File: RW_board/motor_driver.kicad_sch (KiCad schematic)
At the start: 24 parts, among them IC1 MCT8316Z0RQRGFRQ1

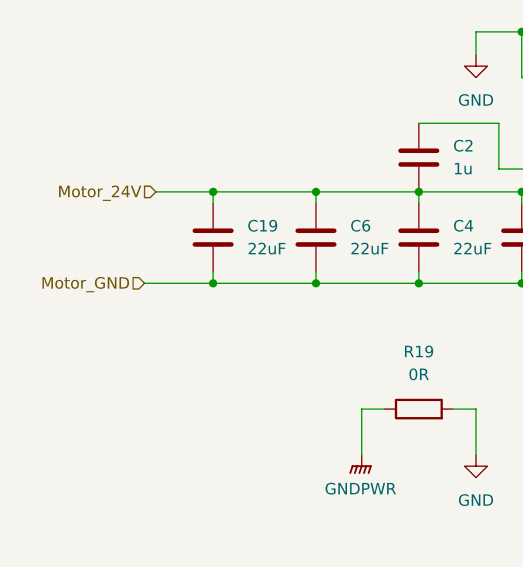
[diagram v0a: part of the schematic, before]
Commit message: Connected everything, added testpoints
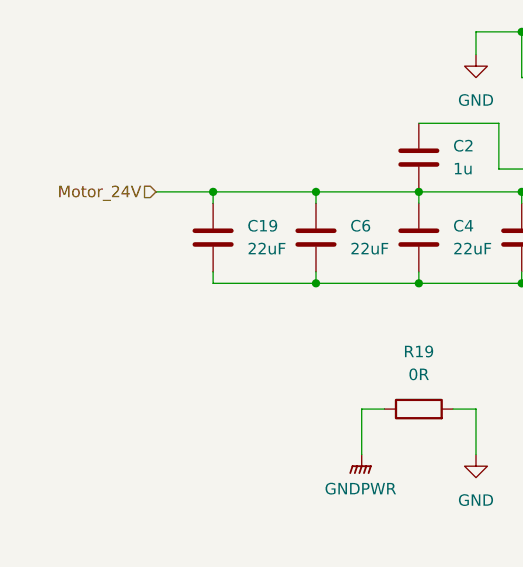
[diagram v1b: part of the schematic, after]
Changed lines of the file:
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@@
-	)
-	(junction
-		(at 81.28 106.68)
-		(diameter 0)
-		(color 0 0 0 0)
 	)
 	(junction
@@
 	(wire
 		(pts
+			(xy 165.1 83.82) (xy 170.18 83.82)
+		)
+		(stroke
+			(width 0)
+			(type default)
+		)
+	)
+	(wire
+		(pts
 			(xy 170.18 45.72) (xy 170.18 48.26)
 		)
@@
 	(wire
 		(pts
-			(xy 73.66 106.68) (xy 81.28 106.68)
-		)
-		(stroke
-			(width 0)
-			(type default)
-		)
-	)
-	(wire
-		(pts
 			(xy 97.79 120.65) (xy 100.33 120.65)
 		)
@@
 		(pts
 			(xy 152.4 121.92) (xy 152.4 124.46)
-		)
-		(stroke
-			(width 0)
-			(type default)
-		)
-	)
-	(wire
-		(pts
-			(xy 165.1 83.82) (xy 170.18 83.82)
 		)
 		(stroke
@@
 	(label "FB_BK"
 		(at 121.92 81.28 0)
-		(fields_autoplaced yes)
 		(effects
 			(font
@@
 	(label "SW_BK"
 		(at 224.79 105.41 0)
-		(fields_autoplaced yes)
 		(effects
 			(font
@@
 	(label "SW_BK"
 		(at 121.92 86.36 0)
-		(fields_autoplaced yes)
 		(effects
 			(font
@@
 	(label "FB_BK"
 		(at 252.73 105.41 180)
-		(fields_autoplaced yes)
 		(effects
 			(font
@@
 		(shape input)
 		(at 198.12 60.96 180)
-		(fields_autoplaced yes)
 		(effects
 			(font
@@
 		(shape output)
 		(at 205.74 114.3 180)
-		(fields_autoplaced yes)
 		(effects
 			(font
@@
 		(shape input)
 		(at 170.18 88.9 0)
-		(fields_autoplaced yes)
 		(effects
 			(font
@@
 		(shape input)
 		(at 144.78 43.18 180)
-		(fields_autoplaced yes)
 		(effects
 			(font
@@
 		(shape input)
 		(at 144.78 53.34 90)
-		(fields_autoplaced yes)
 		(effects
 			(font
@@
 		(shape output)
 		(at 160.02 54.61 0)
-		(fields_autoplaced yes)
 		(effects
 			(font
@@
 		(shape input)
 		(at 74.93 96.52 180)
-		(fields_autoplaced yes)
 		(effects
 			(font
@@
 		(shape output)
 		(at 130.81 43.18 180)
-		(fields_autoplaced yes)
 		(effects
 			(font
@@
 		(shape output)
 		(at 247.65 88.9 180)
-		(fields_autoplaced yes)
 		(effects
 			(font
@@
 		(shape output)
 		(at 129.54 132.08 180)
-		(fields_autoplaced yes)
 		(effects
 			(font
@@
 		(shape input)
 		(at 152.4 53.34 90)
-		(fields_autoplaced yes)
 		(effects
 			(font
@@
 		(shape input)
 		(at 170.18 83.82 0)
-		(fields_autoplaced yes)
 		(effects
 			(font
@@
 		(shape output)
 		(at 195.58 101.6 0)
-		(fields_autoplaced yes)
 		(effects
 			(font
@@
 		(shape input)
 		(at 256.54 105.41 0)
-		(fields_autoplaced yes)
 		(effects
 			(font
@@
 		(shape input)
 		(at 142.24 53.34 90)
-		(fields_autoplaced yes)
 		(effects
 			(font
@@
 		(shape output)
 		(at 247.65 60.96 180)
-		(fields_autoplaced yes)
 		(effects
 			(font
@@
 		(shape output)
 		(at 129.54 134.62 180)
-		(fields_autoplaced yes)
 		(effects
 			(font
@@
 		(shape input)
 		(at 170.18 78.74 0)
-		(fields_autoplaced yes)
 		(effects
 			(font
@@
 		(shape output)
 		(at 195.58 93.98 0)
-		(fields_autoplaced yes)
 		(effects
 			(font
@@
 		(shape input)
 		(at 170.18 104.14 0)
-		(fields_autoplaced yes)
 		(effects
 			(font
@@
 			)
 			(justify left)
-		)
-	)
-	(hierarchical_label "Motor_GND"
-		(shape input)
-		(at 73.66 106.68 180)
-		(fields_autoplaced yes)
-		(effects
-			(font
-				(size 1.27 1.27)
-			)
-			(justify right)
 		)
 	)
@@
 		(shape input)
 		(at 170.18 99.06 0)
-		(fields_autoplaced yes)
 		(effects
 			(font
@@
 		(shape output)
 		(at 210.82 60.96 180)
-		(fields_autoplaced yes)
 		(effects
 			(font
@@
 		(shape output)
 		(at 130.81 33.02 180)
-		(fields_autoplaced yes)
 		(effects
 			(font
@@
 		(shape input)
 		(at 231.14 60.96 180)
-		(fields_autoplaced yes)
 		(effects
 			(font
@@
 		(shape output)
 		(at 129.54 129.54 180)
-		(fields_autoplaced yes)
 		(effects
 			(font
@@
 		(shape input)
 		(at 154.94 53.34 90)
-		(fields_autoplaced yes)
-		(effects
-			(font
+		(effects
+			(font

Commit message: Initial board layout
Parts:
- removed L1: 47uH, Inductor_SMD:L_1210_3225Metric, symbol Device:L
- added L301: BCL322515RT-470M-D, RW_Imports:INDPM3225X150N, symbol RW_Imports:BCL322515RT-470M-D
- C309: renamed from C7; Voltage rating 30V -> 35V
- renumbered C19 to C301, C6 to C302, C2 to C303, C4 to C304, C3 to C305, C1 to C306, C21 to C307, C5 to C308, D6 to D301, D1 to D302, D2 to D303, D3 to D304, IC1 to IC301, R19 to R301, R1 to R302, R4 to R303, R7 to R304, R2 to R305, R3 to R306, R8 to R307, R9 to R308, R10 to R309
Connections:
- net 5V: now also L301.2
- net SW_BK: now also L301.1

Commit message: Initial routing complete
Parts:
- removed R301: 0R, Capacitor_SMD:C_0201_0603Metric, symbol Device:R
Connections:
- net GNDPWR is gone; now on net GND: C301.2, C302.2, C304.2, C305.2, D303.1 (K), IC301.12 (PGND_1), IC301.15 (PGND_2), IC301.18 (PGND_3)
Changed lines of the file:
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@@
 	(wire
 		(pts
-			(xy 97.79 120.65) (xy 100.33 120.65)
+			(xy 97.79 120.65) (xy 110.49 120.65)
 		)
 		(stroke
@@
 		(pts
 			(xy 142.24 127) (xy 148.59 127)
-		)
-		(stroke
-			(width 0)
-			(type default)
-		)
-	)
-	(wire
-		(pts
-			(xy 107.95 120.65) (xy 110.49 120.65)
 		)
 		(stroke
@@
 	(label "FB_BK"
 		(at 121.92 81.28 0)
-		(fields_autoplaced yes)
 		(effects
 			(font
@@
 	(label "SW_BK"
 		(at 212.09 105.41 0)
-		(fields_autoplaced yes)
 		(effects
 			(font
@@
 	(label "SW_BK"
 		(at 121.92 86.36 0)
-		(fields_autoplaced yes)
 		(effects
 			(font
@@
 	(label "FB_BK"
 		(at 252.73 105.41 180)
-		(fields_autoplaced yes)
 		(effects
 			(font
@@
 		(shape input)
 		(at 198.12 60.96 180)
-		(fields_autoplaced yes)
 		(effects
 			(font
@@
 		(shape output)
 		(at 205.74 114.3 180)
-		(fields_autoplaced yes)
 		(effects
 			(font
@@
 		(shape input)
 		(at 170.18 88.9 0)
-		(fields_autoplaced yes)
 		(effects
 			(font
@@
 		(shape input)
 		(at 144.78 43.18 180)
-		(fields_autoplaced yes)
 		(effects
 			(font
@@
 		(shape input)
 		(at 144.78 53.34 90)
-		(fields_autoplaced yes)
 		(effects
 			(font
@@
 		(shape output)
 		(at 160.02 54.61 0)
-		(fields_autoplaced yes)
 		(effects
 			(font
@@
 		(shape input)
 		(at 74.93 96.52 180)
-		(fields_autoplaced yes)
 		(effects
 			(font
@@
 		(shape output)
 		(at 130.81 43.18 180)
-		(fields_autoplaced yes)
 		(effects
 			(font
@@
 		(shape input)
 		(at 176.53 45.72 0)
-		(fields_autoplaced yes)
 		(effects
 			(font
@@
 		(shape output)
 		(at 247.65 88.9 180)
-		(fields_autoplaced yes)
 		(effects
 			(font
@@
 		(shape output)
 		(at 129.54 132.08 180)
-		(fields_autoplaced yes)
 		(effects
 			(font
@@
 		(shape input)
 		(at 152.4 53.34 90)
-		(fields_autoplaced yes)
 		(effects
 			(font
@@
 		(shape input)
 		(at 170.18 83.82 0)
-		(fields_autoplaced yes)
 		(effects
 			(font
@@
 		(shape output)
 		(at 195.58 101.6 0)
-		(fields_autoplaced yes)
 		(effects
 			(font
@@
 		(shape input)
 		(at 256.54 105.41 0)
-		(fields_autoplaced yes)
 		(effects
 			(font
@@
 		(shape input)
 		(at 142.24 53.34 90)
-		(fields_autoplaced yes)
 		(effects
 			(font
@@
 		(shape output)
 		(at 247.65 60.96 180)
-		(fields_autoplaced yes)
 		(effects
 			(font
@@
 		(shape output)
 		(at 129.54 134.62 180)
-		(fields_autoplaced yes)
 		(effects
 			(font
@@
 		(shape input)
 		(at 170.18 78.74 0)
-		(fields_autoplaced yes)
 		(effects
 			(font
@@
 		(shape output)
 		(at 195.58 93.98 0)
-		(fields_autoplaced yes)
 		(effects
 			(font
@@
 		(shape input)
 		(at 170.18 104.14 0)
-		(fields_autoplaced yes)
 		(effects
 			(font
@@
 		(shape input)
 		(at 170.18 99.06 0)
-		(fields_autoplaced yes)
 		(effects
 			(font
@@
 		(shape output)
 		(at 210.82 60.96 180)
-		(fields_autoplaced yes)
 		(effects
 			(font
@@
 		(shape output)
 		(at 130.81 33.02 180)
-		(fields_autoplaced yes)
 		(effects
 			(font
@@
 		(shape input)
 		(at 231.14 60.96 180)
-		(fields_autoplaced yes)
 		(effects
 			(font
@@
 		(shape output)
 		(at 129.54 129.54 180)
-		(fields_autoplaced yes)
 		(effects
 			(font
@@
 		(shape input)
 		(at 154.94 53.34 90)
-		(fields_autoplaced yes)
 		(effects
 			(font
@@
 					(unit 1)
 				)
-			)
-		)
-	)
-	(symbol
-		(lib_id "Device:R")
-		(at 104.14 120.65 90)
-		(unit 1)
-		(exclude_from_sim no)
-		(in_bom yes)
-		(on_board yes)
-		(dnp no)
-		(fields_autoplaced yes)
-		(property "Reference" "R301"
-			(at 104.14 114.3 90)
-			(effects
-				(font
-					(size 1.27 1.27)
-				)
-			)
-		)
-		(property "Value" "0R"
-			(at 104.14 116.84 90)
-			(effects
-				(font
-					(size 1.27 1.27)
-				)
-			)
-		)
-		(property "Footprint" "Capacitor_SMD:C_0201_0603Metric"
-			(at 104.14 122.428 90)
-			(effects
-				(font
-					(size 1.27 1.27)
-				)
-				(hide yes)
-			)
-		)
-		(property "Datasheet" "~"
-			(at 104.14 120.65 0)
-			(effects
-				(font
-					(size 1.27 1.27)
-				)
-				(hide yes)
-			)
-		)
-		(property "Description" "Resistor"
-			(at 104.14 120.65 0)
-			(effects
-				(font
-					(size 1.27 1.27)
-				)
-				(hide yes)
-			)
-		)
-		(pin "1"
-		)
-		(pin "2"
-		)
-		(instances
-			(project ""
-				(path "/ff273890-9ca6-499d-9c73-a93557b69e48/5d0595a1-bd8d-4ee1-8020-62fb85474ed7"
-					(reference "R301")
-					(unit 1)
-				)

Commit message: Add part numbers
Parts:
- C301, C302, C304: Mouser Part Number (none) -> 810-C2012X5R1V226MAC
- C303, C308: Mouser Part Number (none) -> 81-GRM155R6YA105KE1J; Voltage rating 30V -> 35V
- C305, C307: Voltage rating 30V -> 35V
- C306: Voltage Rating 30V -> (none); Voltage rating (none) -> 35V
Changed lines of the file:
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@@
 	(label "FB_BK"
 		(at 121.92 81.28 0)
-		(fields_autoplaced yes)
 		(effects
 			(font
@@
 	(label "SW_BK"
 		(at 212.09 105.41 0)
-		(fields_autoplaced yes)
 		(effects
 			(font
@@
 	(label "SW_BK"
 		(at 121.92 86.36 0)
-		(fields_autoplaced yes)
 		(effects
 			(font
@@
 	(label "FB_BK"
 		(at 252.73 105.41 180)
-		(fields_autoplaced yes)
 		(effects
 			(font
@@
 		(shape input)
 		(at 198.12 60.96 180)
-		(fields_autoplaced yes)
 		(effects
 			(font
@@
 		(shape output)
 		(at 205.74 114.3 180)
-		(fields_autoplaced yes)
 		(effects
 			(font
@@
 		(shape input)
 		(at 170.18 88.9 0)
-		(fields_autoplaced yes)
 		(effects
 			(font
@@
 		(shape input)
 		(at 144.78 43.18 180)
-		(fields_autoplaced yes)
 		(effects
 			(font
@@
 		(shape input)
 		(at 144.78 53.34 90)
-		(fields_autoplaced yes)
 		(effects
 			(font
@@
 		(shape output)
 		(at 160.02 54.61 0)
-		(fields_autoplaced yes)
 		(effects
 			(font
@@
 		(shape input)
 		(at 74.93 96.52 180)
-		(fields_autoplaced yes)
 		(effects
 			(font
@@
 		(shape output)
 		(at 130.81 43.18 180)
-		(fields_autoplaced yes)
 		(effects
 			(font
@@
 		(shape input)
 		(at 176.53 45.72 0)
-		(fields_autoplaced yes)
 		(effects
 			(font
@@
 		(shape output)
 		(at 247.65 88.9 180)
-		(fields_autoplaced yes)
 		(effects
 			(font
@@
 		(shape output)
 		(at 129.54 132.08 180)
-		(fields_autoplaced yes)
 		(effects
 			(font
@@
 		(shape input)
 		(at 152.4 53.34 90)
-		(fields_autoplaced yes)
 		(effects
 			(font
@@
 		(shape input)
 		(at 170.18 83.82 0)
-		(fields_autoplaced yes)
 		(effects
 			(font
@@
 		(shape output)
 		(at 195.58 101.6 0)
-		(fields_autoplaced yes)
 		(effects
 			(font
@@
 		(shape input)
 		(at 256.54 105.41 0)
-		(fields_autoplaced yes)
 		(effects
 			(font
@@
 		(shape input)
 		(at 142.24 53.34 90)
-		(fields_autoplaced yes)
 		(effects
 			(font
@@
 		(shape output)
 		(at 247.65 60.96 180)
-		(fields_autoplaced yes)
 		(effects
 			(font
@@
 		(shape output)
 		(at 129.54 134.62 180)
-		(fields_autoplaced yes)
 		(effects
 			(font
@@
 		(shape input)
 		(at 170.18 78.74 0)
-		(fields_autoplaced yes)
 		(effects
 			(font
@@
 		(shape output)
 		(at 195.58 93.98 0)
-		(fields_autoplaced yes)
 		(effects
 			(font
@@
 		(shape input)
 		(at 170.18 104.14 0)
-		(fields_autoplaced yes)
 		(effects
 			(font
@@
 		(shape input)
 		(at 170.18 99.06 0)
-		(fields_autoplaced yes)
 		(effects
 			(font
@@
 		(shape output)
 		(at 210.82 60.96 180)
-		(fields_autoplaced yes)
 		(effects
 			(font
@@
 		(shape output)
 		(at 130.81 33.02 180)
-		(fields_autoplaced yes)
 		(effects
 			(font
@@
 		(shape input)
 		(at 231.14 60.96 180)
-		(fields_autoplaced yes)
 		(effects
 			(font
@@
 		(shape output)
 		(at 129.54 129.54 180)
-		(fields_autoplaced yes)
 		(effects
 			(font
@@
 		(shape input)
 		(at 154.94 53.34 90)
-		(fields_autoplaced yes)
 		(effects
 			(font
@@
 			)
 		)
-		(property "Voltage rating" "30V"
+		(property "Voltage rating" "35V"
+			(at 104.14 92.71 0)
+			(effects
+				(font
+					(size 1.27 1.27)
+				)
+				(hide yes)
+			)
+		)
+		(property "Mouser Part Number" "81-GRM155R6YA105KE1J "
 			(at 104.14 92.71 0)
 			(effects
@@
 			)
 		)
+		(property "Mouser Part Number" "810-C2012X5R1V226MAC "
+			(at 104.14 101.6 0)
+			(effects
+				(font
+					(size 1.27 1.27)
+				)
+				(hide yes)
+			)
+		)
 		(pin "1"
 		)
@@
 			)
 		)
-		(property "Voltage rating" "30V"
+		(property "Voltage rating" "35V"
 			(at 115.57 101.6 0)
 			(effects
@@
 			)
 		)
-		(property "Voltage rating" "30V"
+		(property "Voltage rating" "35V"
 			(at 170.18 52.07 0)
 			(effects
@@
 			)
 		)
+		(property "Mouser Part Number" "810-C2012X5R1V226MAC "
+			(at 92.71 101.6 0)
+			(effects
+				(font
+					(size 1.27 1.27)
+				)
+				(hide yes)
+			)
+		)
 		(pin "1"
 		)
@@
 			)
 		)
-		(property "Voltage rating" "30V"
+		(property "Voltage rating" "35V"
+			(at 209.55 119.38 0)
+			(effects
+				(font
+					(size 1.27 1.27)
+				)
+				(hide yes)
+			)
+		)
+		(property "Mouser Part Number" "81-GRM155R6YA105KE1J "
 			(at 209.55 119.38 0)
 			(effects
@@
 			)
 		)
+		(property "Mouser Part Number" "810-C2012X5R1V226MAC "
+			(at 81.28 101.6 0)
+			(effects
+				(font
+					(size 1.27 1.27)
+				)
+				(hide yes)
+			)
+		)
 		(pin "1"
 		)
@@
 			)
 		)
-		(property "Voltage Rating" "30V"
+		(property "Voltage Rating" ""
 			(at 121.92 91.44 90)
 			(effects
 				(font
+					(size 1.27 1.27)
+				)
+				(hide yes)
+			)
+		)
+		(property "Voltage rating" "35V"
+			(at 121.92 91.44 0)
+			(effects
+				(font

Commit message: Bom completed and generated, minor PCB adjustments
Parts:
- C305, C307: Mouser Part Number (none) -> 81-GRM155R61H104KE9J
- C306: Mouser Part Number (none) -> 81-GRM155R61H473KE9D
- C309: footprint Capacitor_SMD:C_0402_1005Metric -> Capacitor_SMD:C_0805_2012Metric; Mouser Part Number (none) -> 810-C2012X5R1V226MAC
- D301: Mouser Part Number (none) -> 720-P4112P1R2363X4X5
- D302: Mouser Part Number (none) -> 720-P4112S2U1252X4X5
- D303: Mouser Part Number (none) -> 720-P412Q2T136A8J802
- D304: Mouser Part Number (none) -> 720-P412P1R258A8J802
- R302, R303, R304: Mouser Part Number (none) -> 652-CR0402FX-5101GLF
- R305, R308: Mouser Part Number (none) -> 710-560112110020
- R306, R307, R309: value 330 -> 330R; Mouser Part Number (none) -> 710-560112110231
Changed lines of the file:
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@@
+			)
+		)
+		(property "Mouser Part Number" "652-CR0402FX-5101GLF "
+			(at 149.86 38.1 0)
+			(effects
+				(font
+					(size 1.27 1.27)
+				)
+				(hide yes)
 			)
 		)
@@
 			)
 		)
+		(property "Mouser Part Number" "720-P4112S2U1252X4X5 "
+			(at 213.36 77.47 0)
+			(effects
+				(font
+					(size 1.27 1.27)
+				)
+				(hide yes)
+			)
+		)
 		(pin "1"
 		)
@@
 			)
 		)
-		(property "Footprint" "Capacitor_SMD:C_0402_1005Metric"
+		(property "Footprint" "Capacitor_SMD:C_0805_2012Metric"
 			(at 246.0752 115.57 0)
 			(effects
@@
 		)
 		(property "Voltage rating" "35V"
+			(at 245.11 111.76 0)
+			(effects
+				(font
+					(size 1.27 1.27)
+				)
+				(hide yes)
+			)
+		)
+		(property "Mouser Part Number" "810-C2012X5R1V226MAC "
 			(at 245.11 111.76 0)
 			(effects
@@
 			)
 		)
+		(property "Mouser Part Number" "652-CR0402FX-5101GLF "
+			(at 135.89 38.1 0)
+			(effects
+				(font
+					(size 1.27 1.27)
+				)
+				(hide yes)
+			)
+		)
 		(pin "2"
 		)
@@
 			)
 		)
+		(property "Mouser Part Number" "81-GRM155R61H104KE9J "
+			(at 115.57 101.6 0)
+			(effects
+				(font
+					(size 1.27 1.27)
+				)
+				(hide yes)
+			)
+		)
 		(pin "1"
 		)
@@
 			)
 		)
+		(property "Mouser Part Number" "710-560112110020 "
+			(at 185.42 97.79 0)
+			(effects
+				(font
+					(size 1.27 1.27)
+				)
+				(hide yes)
+			)
+		)
 		(pin "2"
 		)
@@
 			)
 		)
-		(property "Value" "330"
+		(property "Value" "330R"
 			(at 202.438 69.596 0)
 			(effects
@@
 		)
 		(property "Description" "Resistor"
+			(at 200.66 68.58 0)
+			(effects
+				(font
+					(size 1.27 1.27)
+				)
+				(hide yes)
+			)
+		)
+		(property "Mouser Part Number" "710-560112110231 "
 			(at 200.66 68.58 0)
 			(effects
@@
 			)
 		)
+		(property "Mouser Part Number" "720-P412Q2T136A8J802 "
+			(at 232.41 77.47 0)
+			(effects
+				(font
+					(size 1.27 1.27)
+				)
+				(hide yes)
+			)
+		)
 		(pin "1"
 		)
@@
 			)
 		)
+		(property "Mouser Part Number" "81-GRM155R61H104KE9J "
+			(at 170.18 52.07 0)
+			(effects
+				(font
+					(size 1.27 1.27)
+				)
+				(hide yes)
+			)
+		)
 		(pin "1"
 		)
@@
 			)
 		)
-		(property "Value" "330"
+		(property "Value" "330R"
 			(at 251.968 69.596 0)
 			(effects
@@
 		)
 		(property "Description" "Resistor"
+			(at 250.19 68.58 0)
+			(effects
+				(font
+					(size 1.27 1.27)
+				)
+				(hide yes)
+			)
+		)
+		(property "Mouser Part Number" "710-560112110231 "
 			(at 250.19 68.58 0)
 			(effects
@@
 			)
 		)
+		(property "Mouser Part Number" "720-P412P1R258A8J802 "
+			(at 250.19 77.47 0)
+			(effects
+				(font
+					(size 1.27 1.27)
+				)
+				(hide yes)
+			)
+		)
 		(pin "1"
 		)
@@
 		)
 		(property "Description" "Resistor"
+			(at 157.48 38.1 0)
+			(effects
+				(font
+					(size 1.27 1.27)
+				)
+				(hide yes)
+			)
+		)
+		(property "Mouser Part Number" "652-CR0402FX-5101GLF "
 			(at 157.48 38.1 0)
 			(effects
@@
 			)
 		)
-		(property "Value" "330"
+		(property "Value" "330R"
 			(at 215.138 69.596 0)
 			(effects
@@
 			)
 		)
+		(property "Mouser Part Number" "710-560112110231 "
+			(at 213.36 68.58 0)
+			(effects
+				(font
+					(size 1.27 1.27)
+				)
+				(hide yes)
+			)
+		)
 		(pin "2"
 		)
@@
 		)
 		(property "Description" "Resistor"
+			(at 232.41 68.58 0)
+			(effects
+				(font
+					(size 1.27 1.27)
+				)
+				(hide yes)
+			)
+		)
+		(property "Mouser Part Number" "710-560112110020 "
 			(at 232.41 68.58 0)
 			(effects
@@
 			)
 		)
+		(property "Mouser Part Number" "720-P4112P1R2363X4X5 "
+			(at 200.66 77.47 0)
+			(effects
+				(font
+					(size 1.27 1.27)
+				)
+				(hide yes)
+			)
+		)
 		(pin "1"
 		)
@@
 			(at 121.92 91.44 0)
 			(effects
+				(font
+					(size 1.27 1.27)
+				)
+				(hide yes)
+			)
+		)
+		(property "Mouser Part Number" "81-GRM155R61H473KE9D "
+			(at 121.92 91.44 0)
+			(effects
